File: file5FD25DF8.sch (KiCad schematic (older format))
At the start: 10 parts, among them U1 TPSM84209RKHT

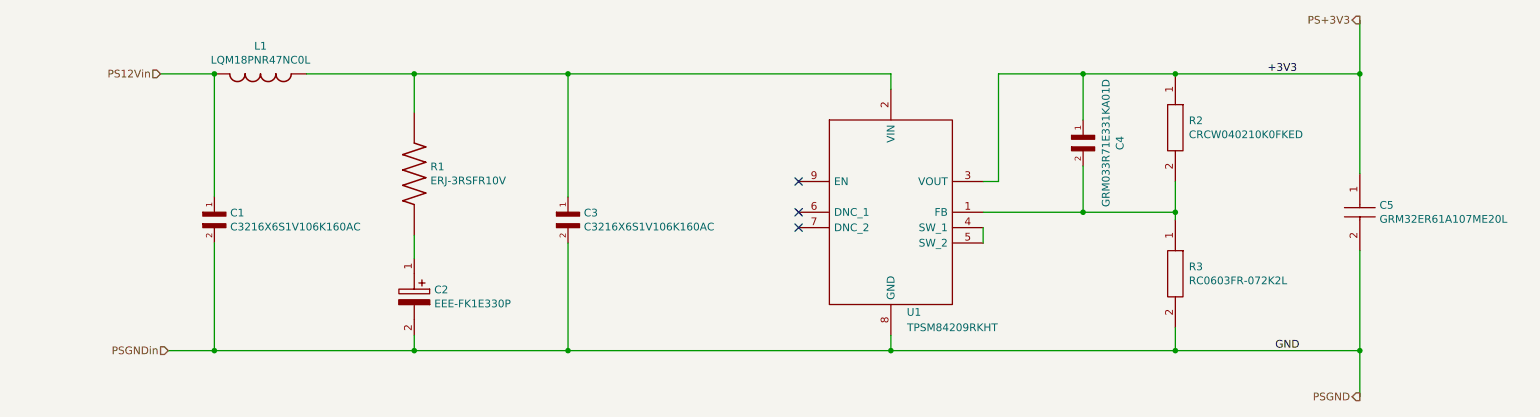
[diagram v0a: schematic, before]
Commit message: Expand hierarchy, reorganize
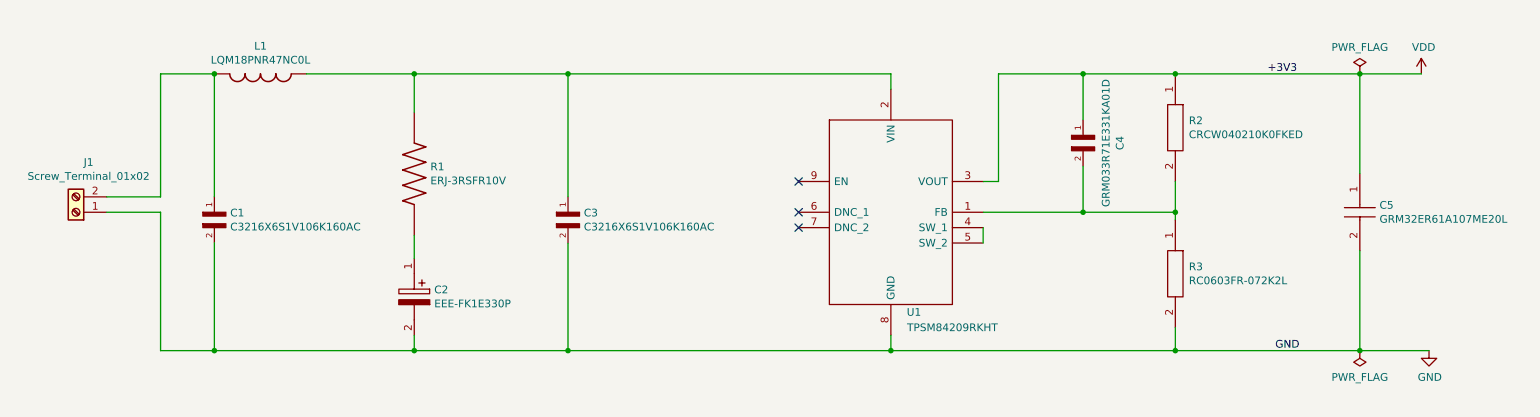
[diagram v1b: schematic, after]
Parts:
- added J1: Screw_Terminal_01x02, symbol Connector:Screw_Terminal_01x02
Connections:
- net PS+3V3 renamed VDD
- net PS12Vin: no longer names the net of C1.1, L1.1
- net PS12Vin: now also J1.2 (Pin_2)
- net PSGND renamed GND
- net GND: now also J1.1 (Pin_1)
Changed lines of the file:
@@
 $Descr A4 11693 8268
 encoding utf-8
-Sheet 2 2
+Sheet 2 4
 Title "KQ9P Power Controller 12VDC"
 Date "2020-12-08"
@@
 	3200 2800 4200 2800
 Wire Wire Line
-	1600 4600 1900 4600
+	1550 4600 1900 4600
 Wire Wire Line
 	1900 2800 1900 3600
@@
 Wire Wire Line
 	9350 3450 9350 2800
-Text HLabel 9350 2450 0    50   Output ~ 0
-PS+3V3
-Wire Wire Line
-	9350 2450 9350 2800
 Connection ~ 9350 2800
-Text HLabel 9350 4900 0    50   Output ~ 0
-PSGND
-Wire Wire Line
-	9350 4900 9350 4600
 Connection ~ 9350 4600
-Text HLabel 1550 2800 0    50   Input ~ 0
-PS12Vin
-Text HLabel 1600 4600 0    50   Input ~ 0
-PSGNDin
 Text Label 8750 2800 0    50   ~ 0
 +3V3
@@
 	6900 3700 7550 3700
 Connection ~ 7550 3700
+$Comp
+L Connector:Screw_Terminal_01x02 J1
+U 1 1 5FE1E454
+P 1000 3700
+F 0 "J1" H 918 3375 50  0000 C CNN
+F 1 "Screw_Terminal_01x02" H 918 3466 50  0000 C CNN
+F 2 "" H 1000 3700 50  0001 C CNN
+F 3 "~" H 1000 3700 50  0001 C CNN
+	1    1000 3700
+	-1   0    0    1
+$EndComp
+Wire Wire Line
+	1200 3600 1550 3600
+Wire Wire Line
+	1550 3600 1550 2800
+Wire Wire Line
+	1200 3700 1550 3700
+Wire Wire Line
+	1550 3700 1550 4600
+$Comp
+L power:VDD #PWR04
+U 1 1 5FE213FA
+P 9750 2800
+F 0 "#PWR04" H 9750 2650 50  0001 C CNN
+F 1 "VDD" H 9765 2973 50  0000 C CNN
+F 2 "" H 9750 2800 50  0001 C CNN
+F 3 "" H 9750 2800 50  0001 C CNN
+	1    9750 2800
+	1    0    0    -1
+$EndComp
+$Comp
+L power:GND #PWR05
+U 1 1 5FE21883
+P 9800 4600
+F 0 "#PWR05" H 9800 4350 50  0001 C CNN
+F 1 "GND" H 9805 4427 50  0000 C CNN
+F 2 "" H 9800 4600 50  0001 C CNN
+F 3 "" H 9800 4600 50  0001 C CNN
+	1    9800 4600
+	1    0    0    -1
+$EndComp
+Wire Wire Line
+	9350 2800 9750 2800
+Wire Wire Line
+	9800 4600 9350 4600
+$Comp
+L power:PWR_FLAG #FLG01
+U 1 1 5FE24C38
+P 9350 2800
+F 0 "#FLG01" H 9350 2875 50  0001 C CNN
+F 1 "PWR_FLAG" H 9350 2973 50  0000 C CNN
+F 2 "" H 9350 2800 50  0001 C CNN
+F 3 "~" H 9350 2800 50  0001 C CNN
+	1    9350 2800
+	1    0    0    -1
+$EndComp
+$Comp
+L power:PWR_FLAG #FLG02
+U 1 1 5FE25169
+P 9350 4600
+F 0 "#FLG02" H 9350 4675 50  0001 C CNN
+F 1 "PWR_FLAG" H 9350 4773 50  0000 C CNN
+F 2 "" H 9350 4600 50  0001 C CNN
+F 3 "~" H 9350 4600 50  0001 C CNN
+	1    9350 4600
+	-1   0    0    1
+$EndComp
 $EndSCHEMATC
